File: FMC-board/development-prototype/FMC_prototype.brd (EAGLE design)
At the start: 103.8 x 69.8 mm, 69 parts, among them J1 DC_POWER_JACK-PJ-102AH, J2 DC_POWER_JACK-PJ-102AH

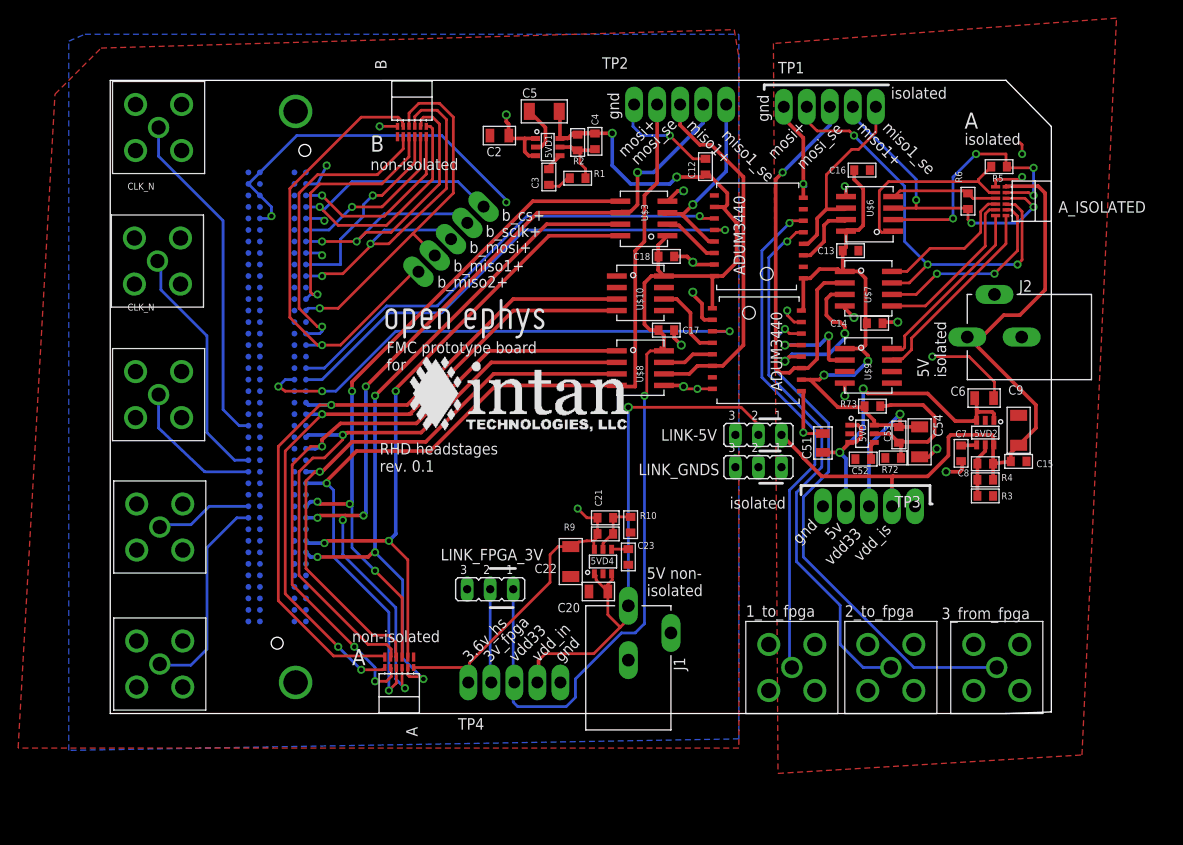
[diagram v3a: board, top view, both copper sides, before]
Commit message: clearing all but layer setup and silkscreen overlap warnings
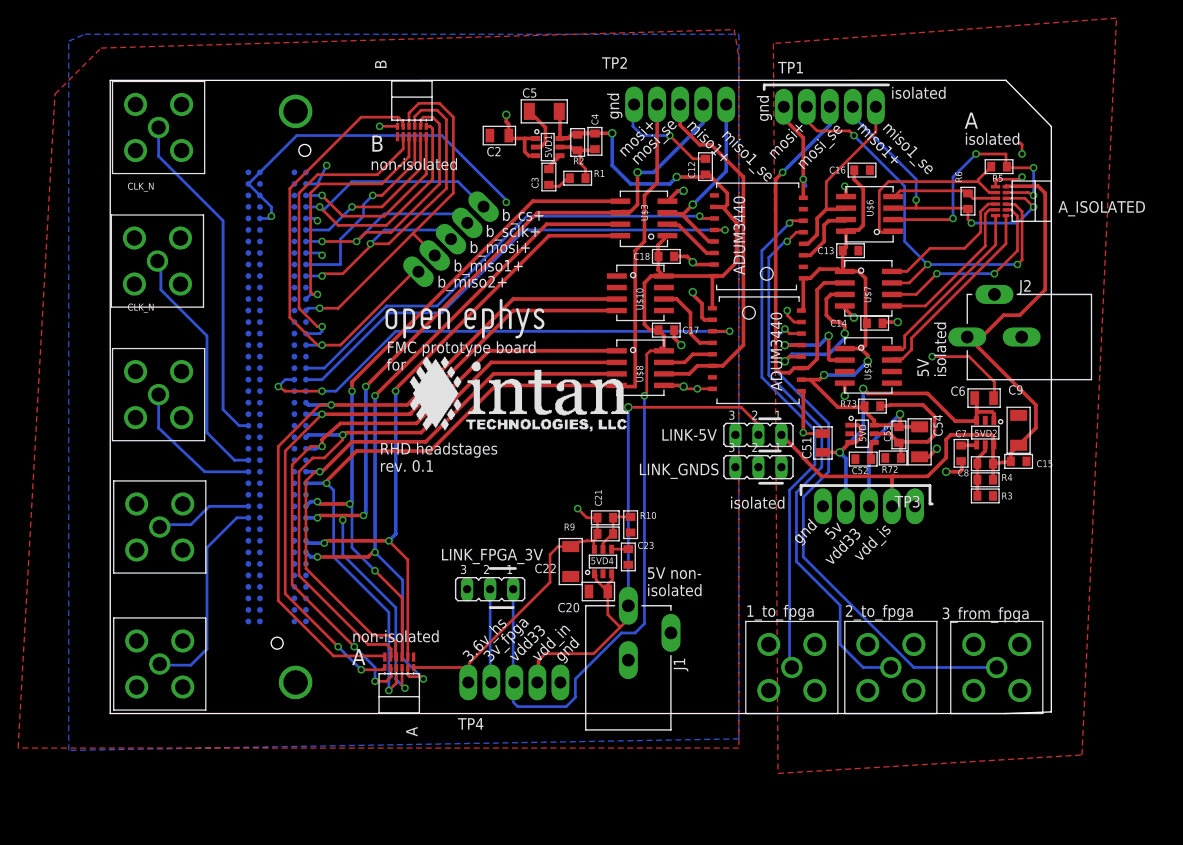
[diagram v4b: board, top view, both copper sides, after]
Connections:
- removed net GND4: C15.2
- net GND_ISOLATED: now also C15.2
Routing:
- net GND: track 94.2 -> 93.7 mm
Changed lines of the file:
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@@
 <layers>
 <layer number="1" name="Top" color="12" fill="1" visible="yes" active="yes"/>
-<layer number="2" name="$GND" color="2" fill="1" visible="no" active="yes"/>
-<layer number="15" name="$VCC" color="3" fill="1" visible="no" active="yes"/>
-<layer number="16" name="Bottom" color="1" fill="1" visible="no" active="yes"/>
+<layer number="2" name="$GND" color="2" fill="1" visible="yes" active="yes"/>
+<layer number="15" name="$VCC" color="3" fill="1" visible="yes" active="yes"/>
+<layer number="16" name="Bottom" color="1" fill="1" visible="yes" active="yes"/>
 <layer number="17" name="Pads" color="2" fill="1" visible="yes" active="yes"/>
 <layer number="18" name="Vias" color="2" fill="1" visible="yes" active="yes"/>
@@
 </class>
 </classes>
-<designrules name="default">
+<designrules name="LaenPCBOrder">
 <description language="de">&lt;b&gt;EAGLE Design Rules&lt;/b&gt;
 &lt;p&gt;
@@
 Einstellungen hier und speichern die Design Rules unter
 einem neuen Namen ab.</description>
-<description language="en">&lt;b&gt;EAGLE Design Rules&lt;/b&gt;
+<description language="en">&lt;b&gt;Laen's PCB Order Design Rules&lt;/b&gt;
 &lt;p&gt;
-The default Design Rules have been set to cover
-a wide range of applications. Your particular design
-may have different requirements, so please make the
-necessary adjustments and save your customized
-design rules under a new name.</description>
+Please make sure your boards conform to these design rules.</description>
 <param name="layerSetup" value="(1*16)"/>
-<param name="mtCopper" value="0.035mm 0.035mm 0.035mm 0.035mm 0.035mm 0.035mm 0.035mm 0.035mm 0.035mm 0.035mm 0.035mm 0.035mm 0.035mm 0.035mm 0.035mm 0.035mm"/>
-<param name="mtIsolate" value="1.5mm 0.15mm 0.2mm 0.15mm 0.2mm 0.15mm 0.2mm 0.15mm 0.2mm 0.15mm 0.2mm 0.15mm 0.2mm 0.15mm 0.2mm"/>
-<param name="mdWireWire" value="8mil"/>
-<param name="mdWirePad" value="8mil"/>
-<param name="mdWireVia" value="8mil"/>
-<param name="mdPadPad" value="8mil"/>
-<param name="mdPadVia" value="8mil"/>
-<param name="mdViaVia" value="8mil"/>
-<param name="mdSmdPad" value="8mil"/>
-<param name="mdSmdVia" value="8mil"/>
-<param name="mdSmdSmd" value="8mil"/>
+<param name="mtCopper" value="0.0356mm 0.0356mm 0.0356mm 0.0356mm 0.0356mm 0.0356mm 0.0356mm 0.0356mm 0.0356mm 0.0356mm 0.0356mm 0.0356mm 0.0356mm 0.0356mm 0.0356mm 0.0356mm"/>
+<param name="mtIsolate" value="1.5011mm 0.1499mm 0.2007mm 0.1499mm 0.2007mm 0.1499mm 0.2007mm 0.1499mm 0.2007mm 0.1499mm 0.2007mm 0.1499mm 0.2007mm 0.1499mm 0.2007mm"/>
+<param name="mdWireWire" value="6mil"/>
+<param name="mdWirePad" value="6mil"/>
+<param name="mdWireVia" value="6mil"/>
+<param name="mdPadPad" value="6mil"/>
+<param name="mdPadVia" value="6mil"/>
+<param name="mdViaVia" value="6mil"/>
+<param name="mdSmdPad" value="6mil"/>
+<param name="mdSmdVia" value="6mil"/>
+<param name="mdSmdSmd" value="6mil"/>
 <param name="mdViaViaSameLayer" value="8mil"/>
 <param name="mnLayersViaInSmd" value="2"/>
-<param name="mdCopperDimension" value="40mil"/>
-<param name="mdDrill" value="8mil"/>
+<param name="mdCopperDimension" value="15mil"/>
+<param name="mdDrill" value="6mil"/>
 <param name="mdSmdStop" value="0mil"/>
-<param name="msWidth" value="10mil"/>
-<param name="msDrill" value="24mil"/>
-<param name="msMicroVia" value="9.99mm"/>
+<param name="msWidth" value="6mil"/>
+<param name="msDrill" value="13mil"/>
+<param name="msMicroVia" value="13mil"/>
 <param name="msBlindViaRatio" value="0.5"/>
 <param name="rvPadTop" value="0.25"/>
@@
 <param name="rvMicroViaOuter" value="0.25"/>
 <param name="rvMicroViaInner" value="0.25"/>
-<param name="rlMinPadTop" value="10mil"/>
+<param name="rlMinPadTop" value="7mil"/>
 <param name="rlMaxPadTop" value="20mil"/>
-<param name="rlMinPadInner" value="10mil"/>
+<param name="rlMinPadInner" value="7mil"/>
 <param name="rlMaxPadInner" value="20mil"/>
-<param name="rlMinPadBottom" value="10mil"/>
+<param name="rlMinPadBottom" value="7mil"/>
 <param name="rlMaxPadBottom" value="20mil"/>
-<param name="rlMinViaOuter" value="8mil"/>
+<param name="rlMinViaOuter" value="7mil"/>
 <param name="rlMaxViaOuter" value="20mil"/>
-<param name="rlMinViaInner" value="8mil"/>
+<param name="rlMinViaInner" value="7mil"/>
 <param name="rlMaxViaInner" value="20mil"/>
 <param name="rlMinMicroViaOuter" value="4mil"/>
@@
 <param name="mvStopFrame" value="1"/>
 <param name="mvCreamFrame" value="0"/>
-<param name="mlMinStopFrame" value="4mil"/>
-<param name="mlMaxStopFrame" value="4mil"/>
+<param name="mlMinStopFrame" value="3mil"/>
+<param name="mlMaxStopFrame" value="3mil"/>
 <param name="mlMinCreamFrame" value="0mil"/>
 <param name="mlMaxCreamFrame" value="0mil"/>
@@
 <vertex x="-4.572" y="74.168"/>
 </polygon>
-<wire x1="21.59" y1="54.61" x2="23.368" y2="54.61" width="0.3048" layer="16"/>
-<wire x1="23.368" y1="54.61" x2="23.622" y2="54.356" width="0.3048" layer="16"/>
-<via x="23.622" y="54.356" extent="1-16" drill="0.5"/>
-<wire x1="23.622" y1="54.356" x2="23.368" y2="54.61" width="0.3048" layer="2"/>
+<wire x1="21.59" y1="54.61" x2="22.606" y2="54.61" width="0.3048" layer="16"/>
+<wire x1="22.606" y1="54.61" x2="22.86" y2="54.356" width="0.3048" layer="16"/>
+<via x="22.86" y="54.356" extent="1-16" drill="0.5"/>
+<wire x1="22.86" y1="54.356" x2="23.368" y2="54.61" width="0.3048" layer="2"/>
 <wire x1="21.59" y1="58.42" x2="22.86" y2="58.42" width="0.3048" layer="16"/>
 <wire x1="22.86" y1="58.42" x2="23.876" y2="60.452" width="0.3048" layer="16"/>
@@
 <wire x1="81.033" y1="55.626" x2="81.16" y2="55.753" width="0.4064" layer="1"/>
 <wire x1="84.455" y1="66.929" x2="84.455" y2="64.135" width="0.3048" layer="1"/>
-<wire x1="84.455" y1="64.135" x2="82.55" y2="62.23" width="0.3048" layer="1"/>
-<wire x1="82.55" y1="62.23" x2="81.788" y2="62.23" width="0.3048" layer="1"/>
-<wire x1="81.788" y1="62.23" x2="78.994" y2="59.436" width="0.3048" layer="1"/>
-<wire x1="78.994" y1="59.436" x2="78.994" y2="55.626" width="0.3048" layer="1"/>
+<wire x1="84.455" y1="64.135" x2="78.994" y2="58.674" width="0.3048" layer="1"/>
+<wire x1="78.994" y1="58.674" x2="78.994" y2="55.626" width="0.3048" layer="1"/>
 </signal>
 <signal name="MISO2-_ISOLATED">
@@
 <wire x1="74.295" y1="66.929" x2="74.295" y2="65.659" width="0.4064" layer="1"/>
 <wire x1="74.295" y1="65.659" x2="76.454" y2="63.5" width="0.4064" layer="1"/>
-<wire x1="76.454" y1="63.5" x2="76.454" y2="58.42" width="0.4064" layer="1"/>
+<wire x1="76.454" y1="63.5" x2="76.454" y2="58.928" width="0.4064" layer="1"/>
 <wire x1="76.235" y1="35.56" x2="76.454" y2="35.56" width="0.4064" layer="1"/>
 <wire x1="76.454" y1="35.56" x2="76.454" y2="30.734" width="0.4064" layer="1"/>
@@
 <wire x1="81.16" y1="58.032" x2="81.026" y2="58.166" width="0.4064" layer="1"/>
 <via x="81.026" y="58.166" extent="1-16" drill="0.5"/>
-<wire x1="76.708" y1="58.166" x2="76.454" y2="58.42" width="0.4064" layer="16"/>
-<via x="76.454" y="58.42" extent="1-16" drill="0.5"/>
-<wire x1="76.454" y1="58.42" x2="76.454" y2="56.896" width="0.4064" layer="1"/>
+<wire x1="76.708" y1="58.166" x2="76.454" y2="58.928" width="0.4064" layer="16"/>
+<via x="76.454" y="58.928" extent="1-16" drill="0.5"/>
+<wire x1="76.454" y1="58.928" x2="76.454" y2="56.896" width="0.4064" layer="1"/>
 <via x="90.678" y="39.37" extent="1-16" drill="0.5"/>
 <wire x1="90.678" y1="39.37" x2="94.742" y2="39.37" width="0.3048" layer="1"/>
@@
 <wire x1="74.676" y1="44.45" x2="74.93" y2="44.704" width="0.3048" layer="2"/>
 <wire x1="74.93" y1="44.704" x2="74.93" y2="45.466" width="0.3048" layer="2"/>
+<contactref element="C15" pad="2"/>
+<wire x1="100.203" y1="32.893" x2="101.0666" y2="27.813" width="0" layer="19" extent="1-1"/>
 </signal>
 <signal name="VDD_ISOLATED">
@@
 <wire x1="97.3836" y1="30.6324" x2="97.282" y2="30.734" width="0.4064" layer="1"/>
 <wire x1="97.282" y1="30.734" x2="92.71" y2="30.734" width="0.4064" layer="1"/>
-<wire x1="92.71" y1="30.734" x2="92.456" y2="30.48" width="0.4064" layer="1"/>
-<wire x1="92.456" y1="30.48" x2="92.456" y2="28.448" width="0.4064" layer="1"/>
-<wire x1="92.456" y1="28.448" x2="90.17" y2="26.162" width="0.4064" layer="1"/>
+<wire x1="92.71" y1="30.734" x2="92.202" y2="30.226" width="0.4064" layer="1"/>
+<wire x1="92.202" y1="30.226" x2="92.202" y2="28.194" width="0.4064" layer="1"/>
+<wire x1="92.202" y1="28.194" x2="90.17" y2="26.162" width="0.4064" layer="1"/>
 <wire x1="90.17" y1="26.162" x2="86.36" y2="26.162" width="0.4064" layer="1"/>
 <wire x1="86.36" y1="26.162" x2="78.486" y2="26.162" width="0.4064" layer="1"/>
@@
 <wire x1="96.52" y1="28.956" x2="96.52" y2="29.638" width="0.4064" layer="1"/>
 </signal>
-<signal name="GND4">
-<contactref element="C15" pad="2"/>
-</signal>
 <signal name="CS+_ISOLATED">

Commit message: added optional DC DC converter
12V > 5V DC DC for powering headstage etc. can still be bypassed with jumper
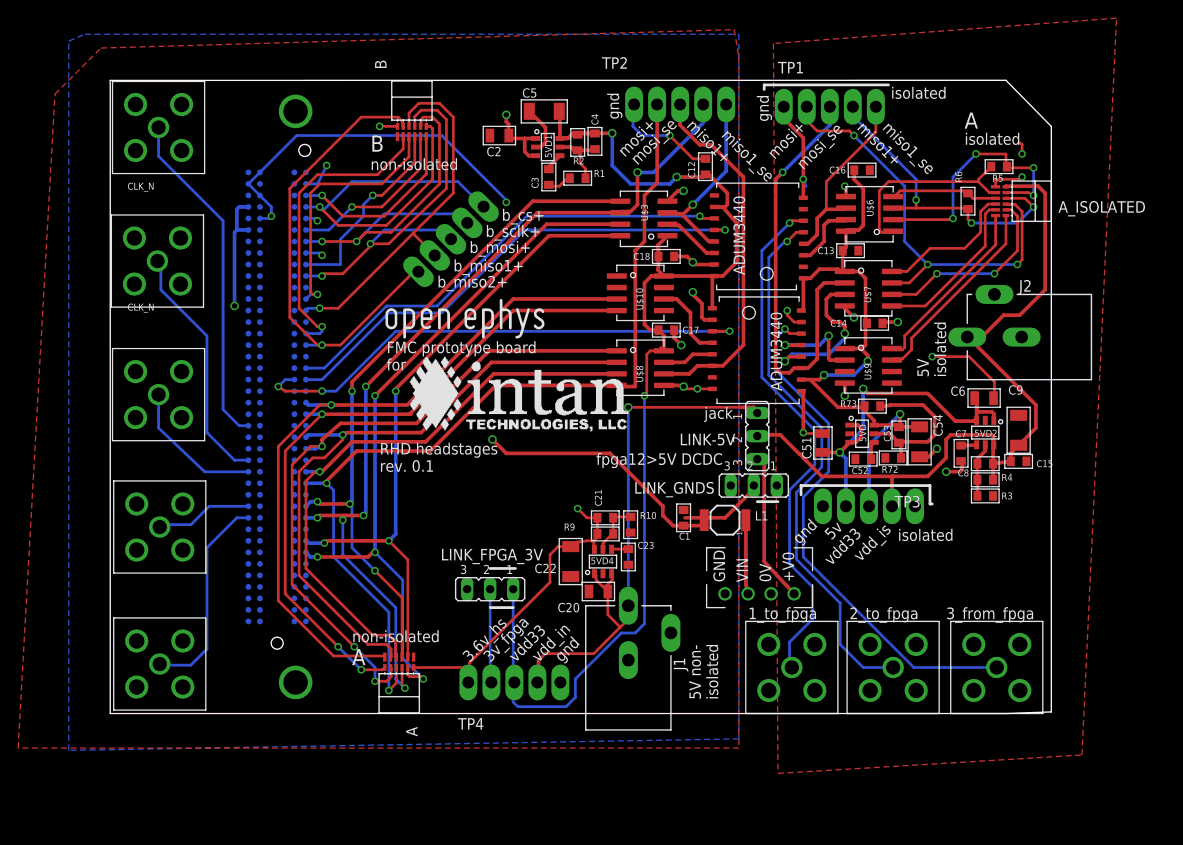
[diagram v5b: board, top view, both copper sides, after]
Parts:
- added C1: 4.7uF, RHD2000_eval_board:0603
- added L1: 6.8uH, inductor-neosid:MS42
- added U$20: PDS1, open-ephys:PDS1
- moved LINK_GNDS 2.09 mm to (71.0, 25.1)
- moved U$19 0.25 mm to (86.4, 5.08)
- moved LINK-5V 0.18 mm to (71.4, 30.6), turned to 270 degrees
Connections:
- new net 12V_FPGA: C1.1, L1.1, U$4.P$155, U$4.P$157
- new net N$1: LINK-5V.3, U$20.P4
- new net N$2: L1.2, U$20.P2
- net GND: now also C1.2, U$20.P1
- net GND_ISOLATED: now also U$20.P3
- net VDD_IN: now also LINK-5V.1; no longer LINK-5V.2
- net VDD_ISOLATED: now also LINK-5V.2; no longer LINK-5V.1
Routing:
- net 12V_FPGA: track 0.00 -> 76.4 mm, vias 0 -> 2
- net N$1: track 0.00 -> 16.5 mm
- net GND: track 93.7 -> 104.7 mm
- net N$2: track 0.00 -> 8.16 mm
- net VDD_ISOLATED: track 82.8 -> 85.5 mm
- net TP2_FROM_SMA: track 55.6 -> 57.7 mm
- net VDD_IN: track 109.8 -> 108.1 mm
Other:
- board text added: "fpga12>5V DCDC"
- board text added: "jack"
